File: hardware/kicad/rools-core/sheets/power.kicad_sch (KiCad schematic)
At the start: 31 parts, among them P1 EURORACK_POWER, P2 EXP_BUS, P3 DEBUG_SWD, U1 AP2112K-3.3, U10 LM393, U2 TPS54302

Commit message: Lay out Core front-panel PCB for 10HP Eurorack fit.
Use RK09L 3-pin no-MP pots, split Daisy daughterboard, audio jack refs, and local display footprint library.

Co-authored-by: Cursor <cursoragent@cursor.com>
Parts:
- removed P1: EURORACK_POWER, Connector_IDC:IDC-Header_2x08_P2.54mm_Vertical, symbol patch-eagle:EURORACK_POWERHEADER
- added J1: EURO_PWR, Connector_IDC:IDC-Header_2x05_P2.54mm_Vertical, symbol Connector_Generic:Conn_02x05_Odd_Even
- renumbered P2 to J2, P3 to J3
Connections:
- net GND: now also J1.8 (Pin_8)
- net at FB2.1: now also J1.2 (Pin_2)
- net at FB1.1: now also J1.10 (Pin_10)
- no-connect marks 1 -> 8
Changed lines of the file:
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@@
 	)
 	(junction
+		(at 46.99 148.59)
+		(diameter 0)
+		(color 0 0 0 0)
+	)
+	(junction
 		(at 132.08 148.59)
 		(diameter 0)
@@
 	)
 	(junction
-		(at 46.99 148.59)
-		(diameter 0)
-		(color 0 0 0 0)
-	)
-	(junction
 		(at 76.2 148.59)
 		(diameter 0)
@@
 	)
 	(no_connect
+		(at 20.32 146.05)
+	)
+	(no_connect
+		(at 20.32 151.13)
+	)
+	(no_connect
+		(at 33.02 153.67)
+	)
+	(no_connect
+		(at 20.32 156.21)
+	)
+	(no_connect
+		(at 20.32 148.59)
+	)
+	(no_connect
+		(at 20.32 153.67)
+	)
+	(no_connect
 		(at 223.52 128.27)
 	)
+	(no_connect
+		(at 33.02 151.13)
+	)
 	(wire
 		(pts
@@
 	(wire
 		(pts
-			(xy 41.91 153.67) (xy 41.91 163.83)
-		)
-		(stroke
-			(width 0)
-			(type default)
-		)
-	)
-	(wire
-		(pts
 			(xy 114.3 162.56) (xy 114.3 168.91)
 		)
@@
 	(wire
 		(pts
-			(xy 41.91 133.35) (xy 41.91 143.51)
+			(xy 41.91 133.35) (xy 41.91 146.05)
 		)
 		(stroke
@@
 	(wire
 		(pts
+			(xy 33.02 156.21) (xy 41.91 156.21)
+		)
+		(stroke
+			(width 0)
+			(type default)
+		)
+	)
+	(wire
+		(pts
 			(xy 35.56 105.41) (xy 46.99 105.41)
 		)
@@
 	(wire
 		(pts
+			(xy 33.02 148.59) (xy 46.99 148.59)
+		)
+		(stroke
+			(width 0)
+			(type default)
+		)
+	)
+	(wire
+		(pts
 			(xy 187.96 45.72) (xy 204.47 45.72)
 		)
@@
 	(wire
 		(pts
+			(xy 33.02 146.05) (xy 41.91 146.05)
+		)
+		(stroke
+			(width 0)
+			(type default)
+		)
+	)
+	(wire
+		(pts
 			(xy 143.51 148.59) (xy 152.4 148.59)
 		)
@@
 	(wire
 		(pts
+			(xy 41.91 156.21) (xy 41.91 163.83)
+		)
+		(stroke
+			(width 0)
+			(type default)
+		)
+	)
+	(wire
+		(pts
 			(xy 101.6 162.56) (xy 137.16 162.56)
 		)
@@
 	(wire
 		(pts
-			(xy 41.91 148.59) (xy 46.99 148.59)
-		)
-		(stroke
-			(width 0)
-			(type default)
-		)
-	)
-	(wire
-		(pts
 			(xy 71.12 133.35) (xy 76.2 133.35)
 		)
@@
 		(dnp no)
 		(fields_autoplaced yes)
-		(property "Reference" "P2"
+		(property "Reference" "J2"
 			(at 181.61 34.29 0)
 			(show_name no)
@@
 			(project "rools-core"
 				(path "/e63e39d7-6ac0-4ffd-8aa3-1841a4541b55/93f4332e-1360-4c3a-9be4-5a5bc27a1424"
-					(reference "P2")
+					(reference "J2")
 					(unit 1)
 					(variant
@@
 		(dnp no)
 		(fields_autoplaced yes)
-		(property "Reference" "P3"
+		(property "Reference" "J3"
 			(at 227.965 39.37 0)
 			(show_name no)
@@
 			(project "rools-core"
 				(path "/e63e39d7-6ac0-4ffd-8aa3-1841a4541b55/93f4332e-1360-4c3a-9be4-5a5bc27a1424"
-					(reference "P3")
+					(reference "J3")
 					(unit 1)
 					(variant
@@
 	)
 	(symbol
-		(lib_id "Device:R")
-		(at 224.79 82.55 90)
+		(lib_id "Connector_Generic:Conn_02x05_Odd_Even")
+		(at 25.4 151.13 0)
+		(mirror x)
 		(unit 1)
 		(body_style 1)
@@
 		(in_pos_files yes)
 		(dnp no)
-		(property "Reference" "R64"
-			(at 224.536 80.264 90)
+		(fields_autoplaced yes)
+		(property "Reference" "J1"
+			(at 26.67 139.7 0)
 			(show_name no)
 			(do_not_autoplace no)
@@
 			)
 		)
-		(property "Value" "10K"
-			(at 224.536 85.09 90)
+		(property "Value" "EURO_PWR"
+			(at 26.67 142.24 0)
 			(show_name no)
 			(do_not_autoplace no)
@@
 			)
 		)
-		(property "Footprint" "Resistor_SMD:R_0603_1608Metric"
-			(at 224.79 84.328 90)
+		(property "Footprint" "Connector_IDC:IDC-Header_2x05_P2.54mm_Vertical"
+			(at 25.4 151.13 0)
 			(hide yes)
 			(show_name no)
@@
 		)
 		(property "Datasheet" ""
-			(at 224.79 82.55 0)
+			(at 25.4 151.13 0)
 			(hide yes)
 			(show_name no)
@@
 			)
 		)
-		(property "Description" "Resistor"
-			(at 224.79 82.55 0)
+		(property "Description" "Generic connector, double row, 02x05, odd/even pin numbering scheme (row 1 odd numbers, row 2 even numbers), script generated (kicad-library-utils/schlib/autogen/connector/)"
+			(at 25.4 151.13 0)
 			(hide yes)
 			(show_name no)
@@
 			)
 		)
-		(property "LCSC" "C25804"
-			(at 224.79 82.55 90)
-			(hide yes)
-			(show_name no)
-			(do_not_autoplace no)
-			(effects
-				(font
-					(size 1.27 1.27)
-				)
-			)
+		(pin "3"
+		)
+		(pin "4"
+		)
+		(pin "8"
+		)
+		(pin "6"
 		)
 		(pin "2"
 		)
+		(pin "5"
+		)
+		(pin "7"
+		)
+		(pin "9"
+		)
 		(pin "1"
 		)
+		(pin "10"
+		)
 		(instances
 			(project "rools-core"
 				(path "/e63e39d7-6ac0-4ffd-8aa3-1841a4541b55/93f4332e-1360-4c3a-9be4-5a5bc27a1424"
-					(reference "R64")
+					(reference "J1")
 					(unit 1)
-					(variant
-						(name "LCSC")
-					)
 				)
 			)
@@
 	)
 	(symbol
-		(lib_id "patch-eagle:EURORACK_POWERHEADER")
-		(at 31.75 146.05 0)
-		(mirror y)
+		(lib_id "Device:R")
+		(at 224.79 82.55 90)
 		(unit 1)
 		(body_style 1)
@@
 		(in_pos_files yes)
 		(dnp no)
-		(property "Reference" "P1"
-			(at 30.226 133.35 0)
+		(property "Reference" "R64"
+			(at 224.536 80.264 90)
 			(show_name no)
 			(do_not_autoplace no)
@@
 			)
 		)
-		(property "Value" "EURORACK_POWER"
-			(at 36.83 158.75 0)
+		(property "Value" "10K"
+			(at 224.536 85.09 90)
 			(show_name no)
 			(do_not_autoplace no)
 			(effects
 				(font
-					(size 1.778 1.5113)
+					(size 1.27 1.27)
 				)
-				(justify left bottom)
 			)
 		)
-		(property "Footprint" "Connector_IDC:IDC-Header_2x08_P2.54mm_Vertical"
-			(at 31.75 146.05 0)
+		(property "Footprint" "Resistor_SMD:R_0603_1608Metric"
+			(at 224.79 84.328 90)
 			(hide yes)
 			(show_name no)
@@
 		)
 		(property "Datasheet" ""
-			(at 31.75 146.05 0)
+			(at 224.79 82.55 0)
 			(hide yes)
 			(show_name no)
@@
 			)
 		)
-		(property "Description" ""
-			(at 31.75 146.05 0)
+		(property "Description" "Resistor"
+			(at 224.79 82.55 0)
 			(hide yes)
 			(show_name no)
@@
 			)
 		)
-		(property "LCSC" "C3406"
-			(at 31.75 146.05 0)
+		(property "LCSC" "C25804"
+			(at 224.79 82.55 90)
 			(hide yes)
 			(show_name no)
@@
 			)
 		)
-		(pin "-12V1"
-		)
-		(pin "+12V1"
+		(pin "2"
 		)
-		(pin "GND5"
+		(pin "1"
 		)
 		(instances
 			(project "rools-core"
 				(path "/e63e39d7-6ac0-4ffd-8aa3-1841a4541b55/93f4332e-1360-4c3a-9be4-5a5bc27a1424"
-					(reference "P1")
+					(reference "R64")
 					(unit 1)
 					(variant

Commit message: Route Core PCB and place Daisy Seed on the daughterboard.
Sync schematic sheets with the split-board layout and updated interconnects.

Co-authored-by: Cursor <cursoragent@cursor.com>
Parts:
- removed C37: 1000uF/25V, Capacitor_SMD:CP_Elec_10x10.5, symbol Device:C_Polarized
- added C11: 10uF, Capacitor_SMD:C_0603_1608Metric, symbol Device:C
- added C38: 100nF, Capacitor_SMD:C_0603_1608Metric, symbol Device:C
- C36: value 1000uF/25V -> 470uF/25V; footprint Capacitor_SMD:CP_Elec_10x10.5 -> Capacitor_THT:CP_Radial_D8.0mm_P3.50mm; LCSC C49256851 -> C43839
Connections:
- net +12V_SAFE: now also C11.1, C38.2
- net GND: now also J1.3 (Pin_3), J1.4 (Pin_4), J1.5 (Pin_5), J1.6 (Pin_6), J1.7 (Pin_7), C11.2, C38.1
- net -12V_IN: now reaches FB2.1, J1.2 (Pin_2)
- net -12V_IN: now also J1.1 (Pin_1)
- net +12V_IN: now reaches FB1.1, J1.10 (Pin_10)
- net +12V_IN: now also J1.9 (Pin_9)
- no-connect marks 8 -> 1
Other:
- moved on the sheet: C36, J1

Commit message: Remove Patch reference assets and continue Core PCB routing.
Drop imported Patch symbols, local display footprint, and stale BOM CSV while advancing layout and schematic interconnects.

Co-authored-by: Cursor <cursoragent@cursor.com>
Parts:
- L1: LCSC C167874 -> C167208
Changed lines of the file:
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@@
 			)
 		)
-		(property "LCSC" "C167874"
+		(property "LCSC" "C167208"
 			(at 139.7 148.59 90)
 			(hide yes)

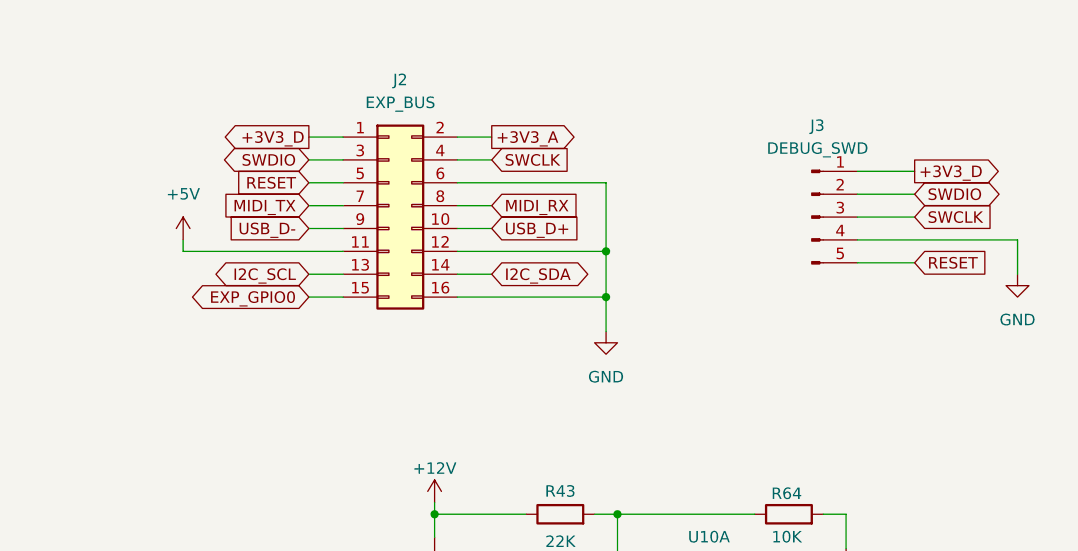
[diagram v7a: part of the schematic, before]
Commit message: Align seed schematic with Electrosmith Daisy module footprint.
Update power and UI interconnects and continue Core PCB layout after removing the local footprint library.

Co-authored-by: Cursor <cursoragent@cursor.com>
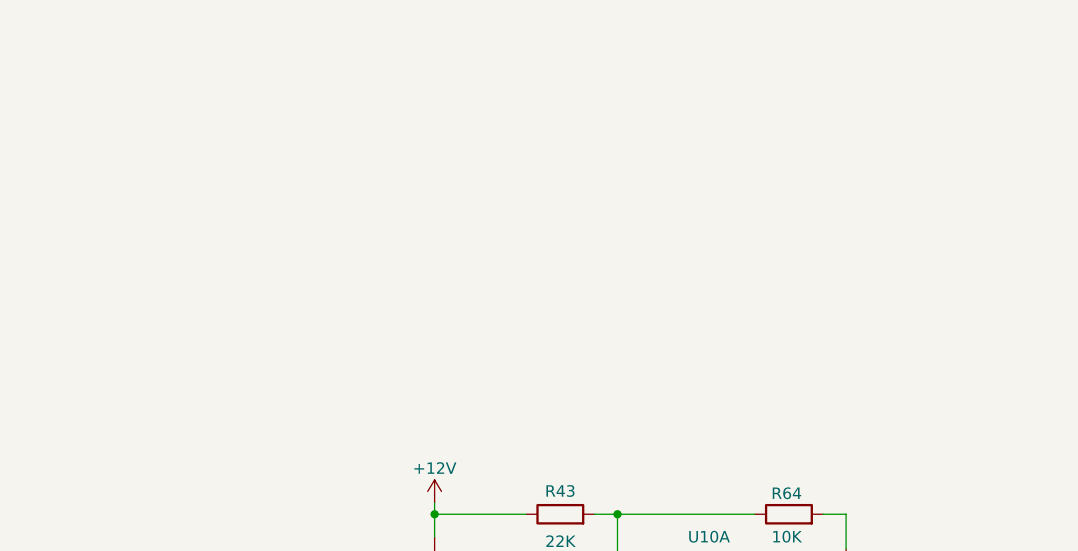
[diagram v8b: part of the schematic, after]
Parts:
- removed J2: EXP_BUS, Connector_PinHeader_2.54mm:PinHeader_2x08_P2.54mm_Vertical, symbol Connector_Generic:Conn_02x08_Odd_Even
- removed J3: DEBUG_SWD, Connector_PinHeader_2.54mm:PinHeader_1x05_P2.54mm_Vertical, symbol Connector:Conn_01x05_Pin
